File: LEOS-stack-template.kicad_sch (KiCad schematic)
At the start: 3 parts

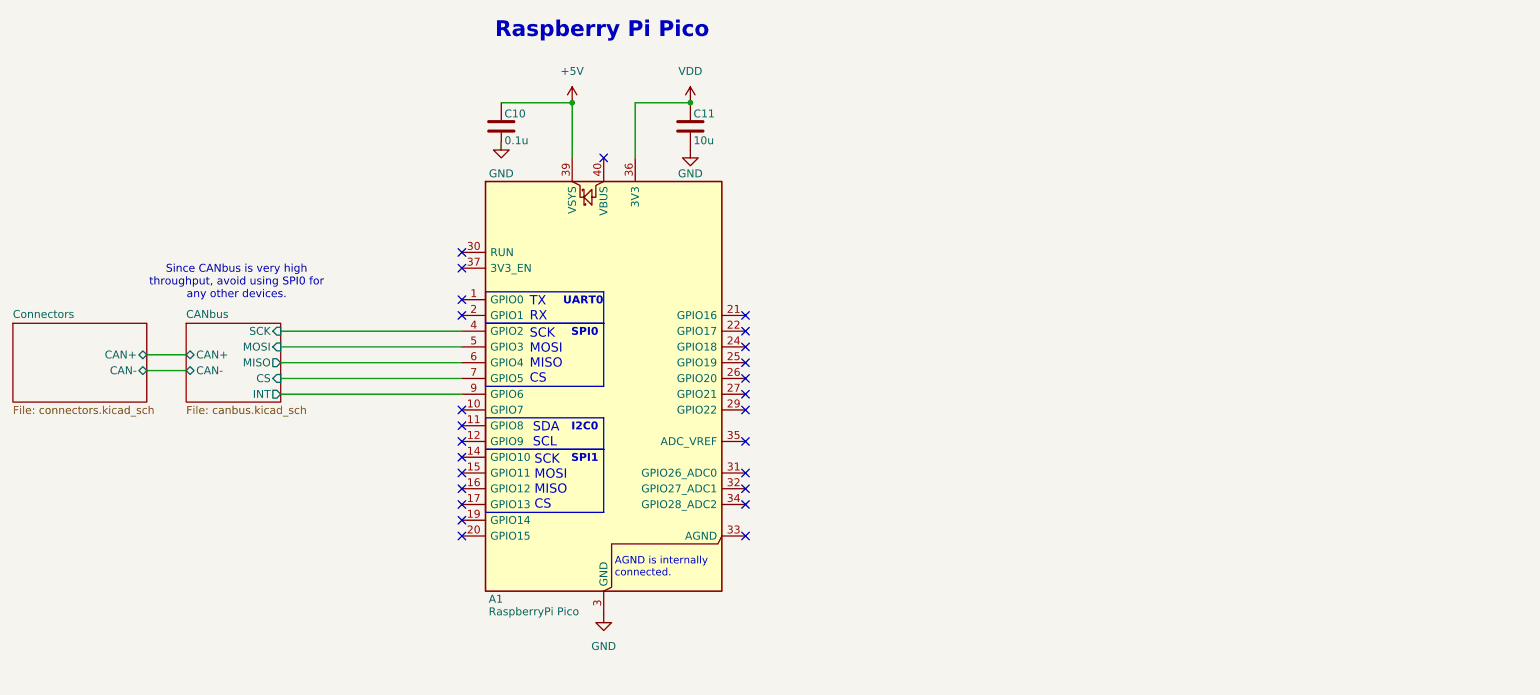
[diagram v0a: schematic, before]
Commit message: Add design help message and bump revision number.
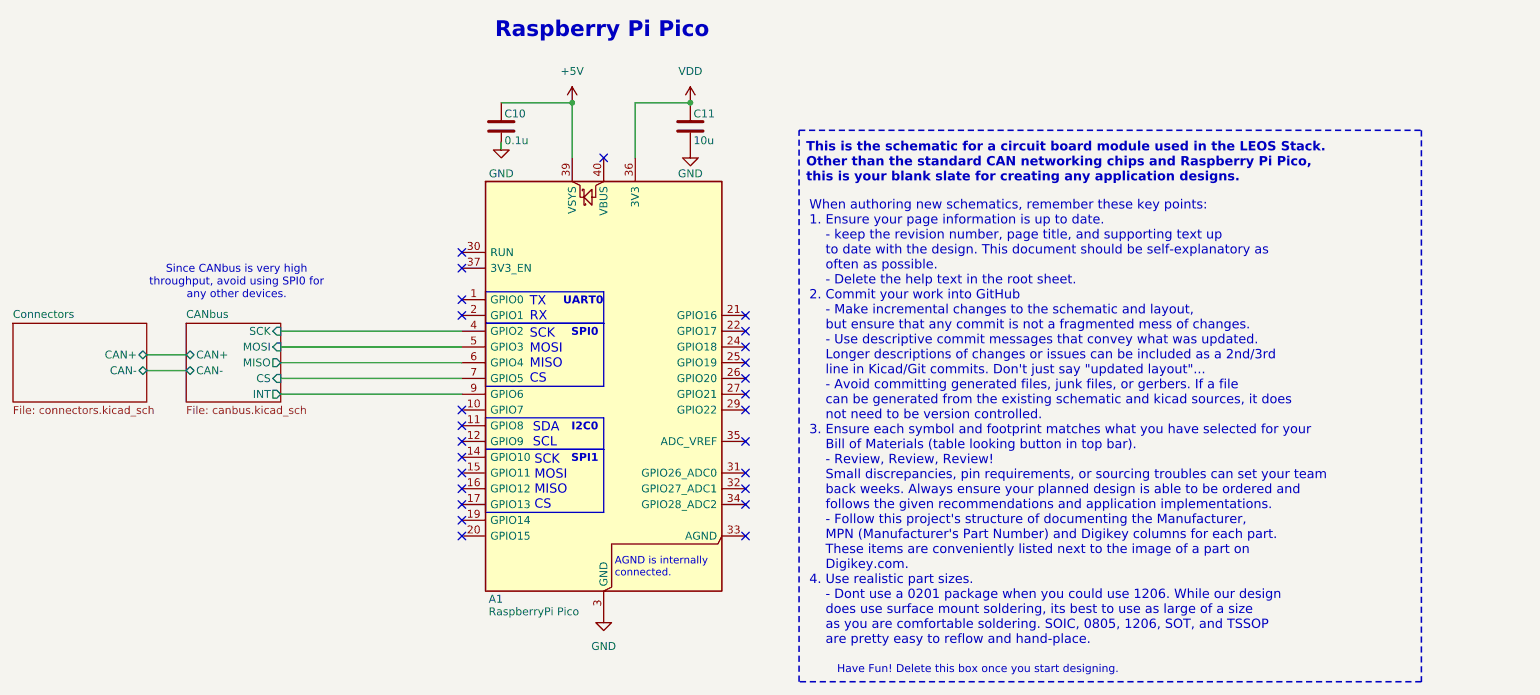
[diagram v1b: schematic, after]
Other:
- note added: "Have Fun! Delete this box once you start designing."
- note added: "This is the schematic for a circuit board module used in the LEOS Stack. Other than the standard CAN networking chips and Raspberry Pi Pico, this is your blank slate for creating any application designs."
- note added: "When authoring new schematics, remember these key points: 1. Ensure your page information is up to date. - keep the revision number, page title, and supporting text up to date with the design. This document should be self-explanatory as often as possible. - Delete the help text in the root sheet. 2. Commit your work into GitHub - Make incremental changes to the schematic and layout, but ensure th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"

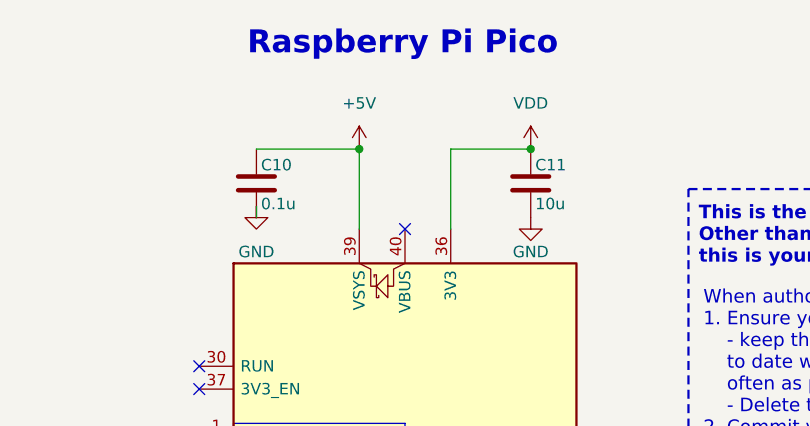
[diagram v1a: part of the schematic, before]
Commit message: Version 3.0
This revision includes a number of changes, notably:
- larger 0805/1206 parts and reduced BOM
- SMD/TH Pads for the Pico Devboard
- Document variable Silkscreen text
- Text documentation throughout schematics
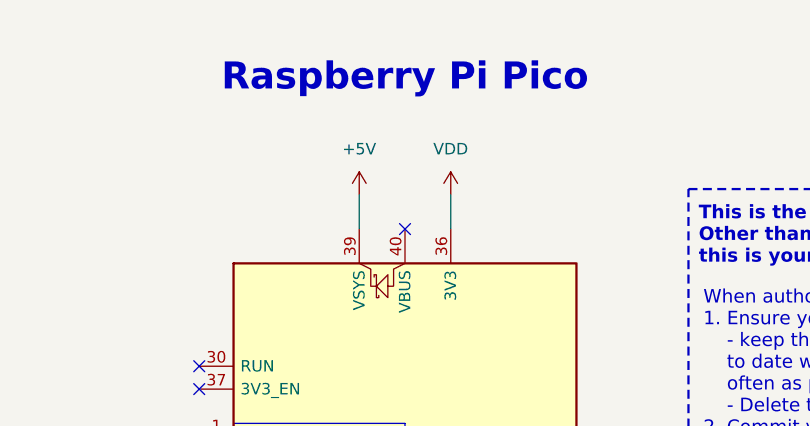
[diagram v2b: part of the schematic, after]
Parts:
- removed C10: 0.1u, Capacitor_SMD:C_0603_1608Metric, symbol Device:C
- removed C11: 10u, Capacitor_SMD:C_0805_2012Metric, symbol Device:C
- A1: footprint Module:RaspberryPi_Pico_Common_THT -> Module:RaspberryPi_Pico_Common_Unspecified
